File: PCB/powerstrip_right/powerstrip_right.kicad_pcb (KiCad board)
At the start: 2 copper layers, 37 x 100 mm, 0 parts

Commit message: random upload
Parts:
- added C1: C, Capacitor_SMD:C_1206_3216Metric_Pad1.33x1.80mm_HandSolder, B.Cu at (156.1, 49.2)
- added C10: C_Polarized, Capacitor_THT:CP_Radial_D5.0mm_P2.50mm, F.Cu at (150.2, 134.1)
- added C11: C_Polarized, Capacitor_THT:CP_Radial_D5.0mm_P2.50mm, F.Cu at (153.0, 60.0)
- added C3: C_Polarized, Capacitor_THT:CP_Radial_D5.0mm_P2.50mm, F.Cu at (132.2, 128.5)
- added C4: C_Polarized, Capacitor_THT:CP_Radial_D5.0mm_P2.50mm, F.Cu at (138.9, 134.1)
- added C5: C_Polarized, Capacitor_THT:CP_Radial_D5.0mm_P2.50mm, F.Cu at (153.0, 54.2)
- added C6: C_Polarized, Capacitor_THT:CP_Radial_D5.0mm_P2.50mm, F.Cu at (156.8, 129.0)
- added C7: C_Polarized, Capacitor_THT:CP_Radial_D5.0mm_P2.50mm, F.Cu at (144.6, 134.1)
- added C8: C_Polarized, Capacitor_THT:CP_Radial_D5.0mm_P2.50mm, F.Cu at (136.0, 60.0)
- added C9: C_Polarized, Capacitor_THT:CP_Radial_D5.0mm_P2.50mm, F.Cu at (132.2, 122.9)
- added IC1: PCA9685PW_Q900,118, Power_Strip_Library:SOP65P640X110-28N, B.Cu at (140.7, 45.5)
- added J1: XT60PW-M, Power_Strip_Library:AMASS_XT60PW-M, F.Cu at (145.0, 105.9)
- added J2: Conn_01x06_Pin, Connector_PinHeader_2.54mm:PinHeader_1x06_P2.54mm_Vertical, F.Cu at (138.2, 128.2)
- added J3: Conn_01x06_Pin, Connector_PinHeader_2.54mm:PinHeader_1x06_P2.54mm_Vertical, F.Cu at (138.2, 125.7)
- added J4: Conn_01x06_Pin, Connector_PinHeader_2.54mm:PinHeader_1x06_P2.54mm_Vertical, F.Cu at (138.2, 123.1)
- added J5: Conn_01x03_Pin, Connector_PinHeader_2.54mm:PinHeader_1x03_P2.54mm_Vertical, F.Cu at (141.9, 55.2)
- added J6: Conn_01x03_Pin, Connector_PinHeader_2.54mm:PinHeader_1x03_P2.54mm_Vertical, F.Cu at (144.5, 55.2)
- added J7: Conn_01x03_Pin, Connector_PinHeader_2.54mm:PinHeader_1x03_P2.54mm_Vertical, F.Cu at (147.1, 55.2)
- added J8: Conn_01x08_Pin, Connector_FFC-FPC:Amphenol_F32Q-1A7x1-11008_1x08-1MP_P0.5mm_Horizontal, B.Cu at (128.8, 53.5)
- added J9: Conn_01x02_Pin, Connector_JST:JST_XH_B2B-XH-AM_1x02_P2.50mm_Vertical, F.Cu at (160.1, 58.0)
- added U1: MUX508IDR, Power_Strip_Library:SOIC127P600X175-16N, B.Cu at (150.4, 45.5)
- added U2: INA181, Package_TO_SOT_SMD:SOT-23-6, B.Cu at (159.7, 49.8)
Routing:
- added copper zone on B.Cu, net GND
- added copper zone on F.Cu, net VCC

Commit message: Stripe PCB's
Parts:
- added C12: 100n, Capacitor_SMD:C_0201_0603Metric_Pad0.64x0.40mm_HandSolder, B.Cu at (160.0, 59.6)
- added C13: 100n, Capacitor_SMD:C_0201_0603Metric_Pad0.64x0.40mm_HandSolder, B.Cu at (159.5, 47.7)
- added C14: 1u, Capacitor_SMD:C_1206_3216Metric_Pad1.33x1.80mm_HandSolder, F.Cu at (154.1, 42.8)
- added C15: 10u Tantal, Capacitor_SMD:C_1206_3216Metric_Pad1.33x1.80mm_HandSolder, F.Cu at (150.3, 48.4)
- added C2: 100n, Capacitor_SMD:C_0201_0603Metric_Pad0.64x0.40mm_HandSolder, B.Cu at (153.4, 41.6)
- added U3: LT1117CST-3.3, PCM_Package_TO_SOT_SMD_AKL:SOT-223-3_TabPin2, F.Cu at (148.4, 43.4)
- added shunt: R0.005, Resistor_SMD:R_0201_0603Metric_Pad0.64x0.40mm_HandSolder, B.Cu at (134.2, 60.3)
- added shunt: R0.005, Resistor_SMD:R_0201_0603Metric_Pad0.64x0.40mm_HandSolder, B.Cu at (134.2, 55.2)
- added shunt: R0.005, Resistor_SMD:R_0201_0603Metric_Pad0.64x0.40mm_HandSolder, B.Cu at (150.9, 120.1)
- added shunt: R0.005, Resistor_SMD:R_0201_0603Metric_Pad0.64x0.40mm_HandSolder, B.Cu at (145.8, 120.1)
- added shunt: R0.005, Resistor_SMD:R_0201_0603Metric_Pad0.64x0.40mm_HandSolder, B.Cu at (134.2, 57.8)
- added shunt: R0.005, Resistor_SMD:R_0201_0603Metric_Pad0.64x0.40mm_HandSolder, B.Cu at (140.7, 120.1)
- added shunt: R0.005, Resistor_SMD:R_0201_0603Metric_Pad0.64x0.40mm_HandSolder, B.Cu at (143.2, 120.1)
- added shunt: R0.005, Resistor_SMD:R_0201_0603Metric_Pad0.64x0.40mm_HandSolder, B.Cu at (138.2, 120.1)
- C1: value C -> 100n; footprint Capacitor_SMD:C_1206_3216Metric_Pad1.33x1.80mm_HandSolder -> Capacitor_SMD:C_0201_0603Metric_Pad0.64x0.40mm_HandSolder
- moved J9 26.9 mm to (138.2, 42.4), turned to 0 degrees
- moved U1 14.2 mm to (155.9, 58.5), turned to 0 degrees
- moved J2 13.7 mm to (150.8, 123.0), turned to -90 degrees
- moved J4 13.6 mm to (150.8, 128.1), turned to -90 degrees
- moved J3 12.7 mm to (150.8, 125.5), turned to -90 degrees
- moved C8 10.7 mm to (140.0, 50.0), turned to 180 degrees
- moved IC1 7.60 mm to (148.3, 45.4)
- moved C11 6.97 mm to (146.0, 60.0), turned to 0 degrees
- moved C5 6.92 mm to (146.0, 54.2), turned to 0 degrees
- moved J7 4.51 mm to (142.5, 55.2)
- moved J5 4.51 mm to (137.4, 55.2)
- moved J6 4.51 mm to (140.0, 55.2)
- moved C6 4.08 mm to (154.4, 125.6), turned to 0 degrees
- moved C3 2.55 mm to (134.8, 128.4), turned to 180 degrees
- moved C9 2.40 mm to (134.7, 122.8), turned to 180 degrees
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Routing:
- net PWM_SERVO9: track 0.00 -> 121.6 mm, vias 0 -> 3
- net PWM_SERVO8: track 0.00 -> 118.3 mm, vias 0 -> 3
- net PWM_SERVO7: track 0.00 -> 116.7 mm, vias 0 -> 1
- net PWM_SERVO6: track 0.00 -> 113.0 mm, vias 0 -> 1
- net PWM_SERVO5: track 0.00 -> 109.4 mm, vias 0 -> 1
- net PWM_SERVO4: track 0.00 -> 105.5 mm, vias 0 -> 1
- net GND_SERVO6: track 0.00 -> 97.0 mm, vias 0 -> 2
- net GND_SERVO7: track 0.00 -> 96.4 mm, vias 0 -> 2
- net GND_SERVO8: track 0.00 -> 95.6 mm, vias 0 -> 2
- net GND_SERVO4: track 0.00 -> 90.0 mm, vias 0 -> 2
- net GND_SERVO9: track 0.00 -> 89.6 mm, vias 0 -> 2
- net 3.3V: track 0.00 -> 76.3 mm, vias 0 -> 3
- net ADC INPUT: track 0.00 -> 42.3 mm, vias 0 -> 4
- net A1: track 0.00 -> 41.4 mm, vias 0 -> 2
- net A2: track 0.00 -> 41.4 mm, vias 0 -> 2
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- added copper zone on B.Cu, net VCC
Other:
- board text added: "1"
- board text added: "2"
- board text added: "3"
- board text added: "4"
- board text added: "5"
- board text added: "6"
- board text added: "7"
- board text added: "8"
- board text added: "9"
- board text added: "GND"
- board text added: "PWM"
- board text added: "VCC"

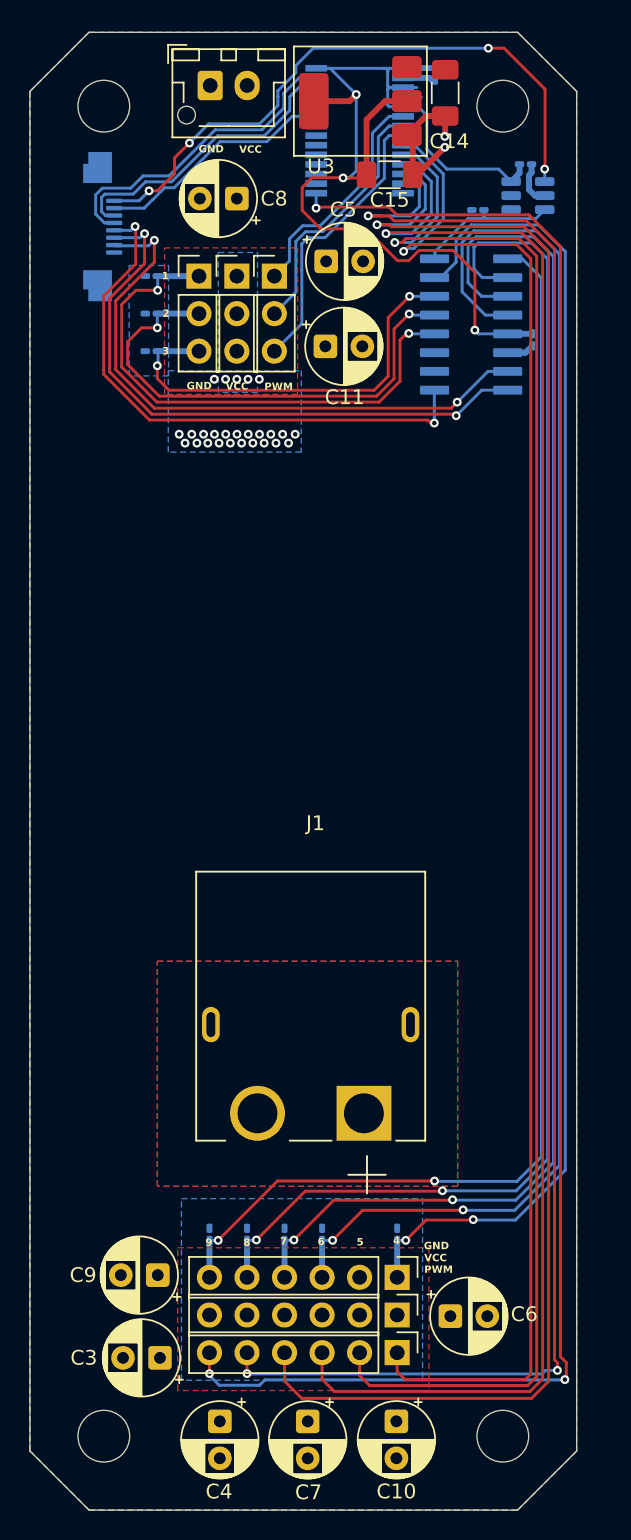
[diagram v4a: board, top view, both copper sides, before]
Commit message: Stop tracking renders folder & final Powerstrip and Mainboard PCB
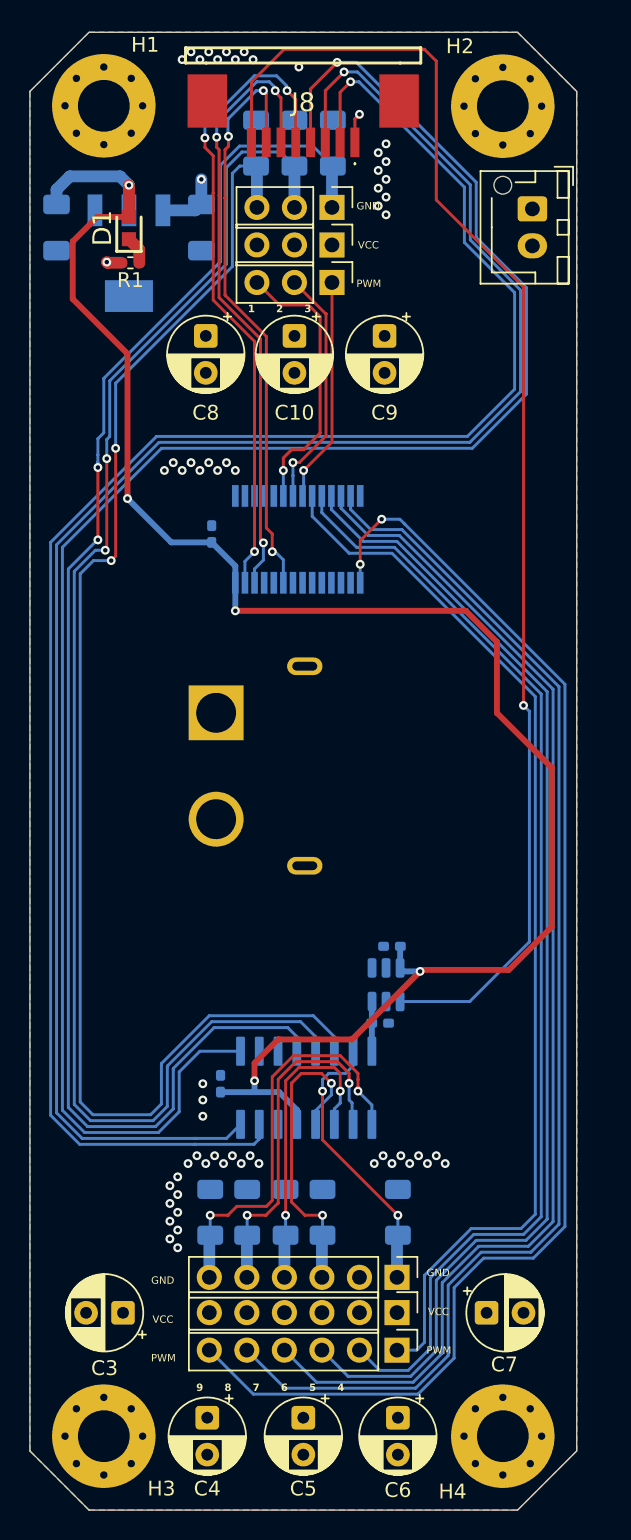
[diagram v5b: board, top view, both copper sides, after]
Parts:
- removed C11: C_Polarized, Capacitor_THT:CP_Radial_D5.0mm_P2.50mm
- removed shunt (x8): R0.005, Resistor_SMD:R_0201_0603Metric_Pad0.64x0.40mm_HandSolder
- added D1: LED, Power_Strip_Library:LEDC1608X70N, F.Cu at (132.7, 52.0)
- added H1: MountingHole_Pad, MountingHole:MountingHole_3.5mm_Pad_Via, F.Cu at (131.0, 43.7)
- added H2: MountingHole_Pad, MountingHole:MountingHole_3.5mm_Pad_Via, F.Cu at (158.0, 43.8)
- added H3: MountingHole_Pad, MountingHole:MountingHole_3.5mm_Pad_Via, F.Cu at (131.0, 133.8)
- added H4: MountingHole_Pad, MountingHole:MountingHole_3.5mm_Pad_Via, F.Cu at (158.0, 133.8)
- added R1: R, Resistor_SMD:R_0402_1005Metric_Pad0.72x0.64mm_HandSolder, F.Cu at (132.8, 54.4)
- added shunt_01: R0.005, Resistor_SMD:R_1206_3216Metric_Pad1.30x1.75mm_HandSolder, B.Cu at (146.5, 46.2)
- added shunt_2: R0.005, Resistor_SMD:R_1206_3216Metric_Pad1.30x1.75mm_HandSolder, B.Cu at (143.9, 46.2)
- added shunt_3: R0.005, Resistor_SMD:R_1206_3216Metric_Pad1.30x1.75mm_HandSolder, B.Cu at (141.3, 46.2)
- added shunt_4: R0.005, Resistor_SMD:R_1206_3216Metric_Pad1.30x1.75mm_HandSolder, B.Cu at (150.9, 118.6)
- added shunt_5: R0.005, Resistor_SMD:R_1206_3216Metric_Pad1.30x1.75mm_HandSolder, B.Cu at (145.8, 118.6)
- added shunt_6: R0.005, Resistor_SMD:R_1206_3216Metric_Pad1.30x1.75mm_HandSolder, B.Cu at (143.3, 118.6)
- added shunt_7: R0.005, Resistor_SMD:R_1206_3216Metric_Pad1.30x1.75mm_HandSolder, B.Cu at (140.7, 118.6)
- added shunt_8: R0.005, Resistor_SMD:R_1206_3216Metric_Pad1.30x1.75mm_HandSolder, B.Cu at (138.2, 118.6)
- C1, C12, C13, C2: footprint Capacitor_SMD:C_0201_0603Metric_Pad0.64x0.40mm_HandSolder -> Capacitor_SMD:C_0402_1005Metric_Pad0.74x0.62mm_HandSolder
- C14, C15, J1: moved to B.Cu
- J8: footprint Connector_FFC-FPC:Amphenol_F32Q-1A7x1-11008_1x08-1MP_P0.5mm_Horizontal -> Power_Strip_Library:17352658; moved to F.Cu
- U3: footprint PCM_Package_TO_SOT_SMD_AKL:SOT-223-3_TabPin2 -> Power_Strip_Library:SOT230P700X180-4N; moved to B.Cu
- moved C5 78.3 mm to (144.5, 132.5), turned to -90 degrees
- moved C10 73.8 mm to (143.9, 59.3)
- moved C9 65.4 mm to (150.0, 59.3), turned to -90 degrees
- moved C1 55.4 mm to (149.7, 105.8), turned to 0 degrees
- moved C12 54.6 mm to (138.9, 109.9), turned to -90 degrees
- moved U2 54.3 mm to (150.1, 103.2), turned to 90 degrees
- moved C13 53.7 mm to (150.5, 100.6), turned to 180 degrees
- moved U1 52.8 mm to (144.7, 110.2), turned to -90 degrees
- moved C2 34.6 mm to (138.3, 72.7), turned to 90 degrees
- moved IC1 28.0 mm to (144.1, 73.1), turned to -90 degrees
- moved J9 23.3 mm to (160.0, 50.7), turned to -90 degrees
- moved C15 22.8 mm to (127.8, 52.0), turned to -90 degrees
- moved C14 18.9 mm to (137.6, 52.0)
- moved U3 18.7 mm to (132.7, 53.7), turned to -90 degrees
- moved J8 18.0 mm to (144.5, 43.0), turned to 180 degrees
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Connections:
- C12 pad 2: 3.3V -> +3.3V
- C13 pad 1: 3.3V -> +3.3V
- C15 pad 1: 3.3V -> +3.3V
- C2 pad 1: 3.3V -> +3.3V
- IC1 pad 1: 3.3V -> GND
- IC1 pad 28: 3.3V -> +3.3V
- IC1 pad 3: 3.3V -> GND
- IC1 pad 5: 3.3V -> GND
- IC1 pad 6: PWM_SERVO1 -> PWM_SERVO3
- IC1 pad 8: PWM_SERVO3 -> PWM_SERVO1
- U1 pad 13: 3.3V -> +3.3V
- U2 pad 6: 3.3V -> +3.3V
- U3 pad 2: 3.3V -> +3.3V
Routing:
- net +3.3V: track 0.00 -> 120.9 mm, vias 0 -> 5
- net A0: track 38.5 -> 125.0 mm, vias 2 -> 1
- net A2: track 41.4 -> 120.8 mm, vias 2 -> 1
- net A1: track 41.4 -> 120.3 mm, vias 2 -> 1
- net 3.3V: track 76.3 -> 0.00 mm, vias 3 -> 0
- net GND_SERVO6: track 97.0 -> 21.2 mm
- net GND_SERVO7: track 96.4 -> 21.2 mm
- net GND_SERVO8: track 95.6 -> 24.2 mm
- net GND_SERVO4: track 90.0 -> 19.0 mm
- net GND_SERVO3: track 28.7 -> 95.9 mm
- net GND_SERVO2: track 33.7 -> 98.9 mm
- net GND_SERVO1: track 36.6 -> 101.2 mm
- net GND_SERVO9: track 89.6 -> 27.9 mm
- net ADC INPUT: track 42.3 -> 90.5 mm, vias 4 -> 1
- net PWM_SERVO7: track 116.7 -> 82.7 mm, vias 1 -> 0
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- added copper zone on In1.Cu, net GND
- added copper zone on In2.Cu, net VCC
- removed copper zone on B.Cu, net VCC
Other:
- outline, holes or cut-outs redrawn
- copper layers 2 -> 4
- board text added: "1 2 3"
- board text added: "9 8 7 6 5 4"
- board text added: "S1"
- board text added: "S2"
- board text added: "S3"
- board text added: "S4"
- board text added: "S6"
- board text added: "S7"
- board text added: "S8"
- board text added: "S9"
- board text removed: "1"
- board text removed: "2"
- board text removed: "3"
- board text removed: "4"
- board text removed: "5"
- board text removed: "6"
- board text removed: "7"
- board text removed: "8"
- board text removed: "9"
